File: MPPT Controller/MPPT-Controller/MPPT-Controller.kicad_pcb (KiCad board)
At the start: 4 copper layers, 81 parts, among them J1 Conn_01x02_Pin, J2 Conn_01x02_Pin, J3 Conn_01x02_Pin, J4 Conn_01x02_Pin, J5 USB_C_Receptacle_USB2.0_16P, J6 Conn_01x02_Pin, M1 Fan_4pin, Q1 IRL540N, SW1 SW_SPDT, U1 ADS1115IDGS, U2 ESP32-WROOM-32D, U3 CH340C, U4 LM1117DT-3.3, U5 LM2596S-ADJ, U6 TC4422, U7 ADS1115IDGS

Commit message: Layout
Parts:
- moved LR4 13.6 mm to (110.6, 106.7), turned to 90 degrees
- moved J2 11.2 mm to (121.9, 118.8)
- moved LR3 4.57 mm to (110.6, 119.0), turned to 90 degrees
- moved D10 1.98 mm to (179.8, 85.1)
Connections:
- HS1 pad 1: GND -> VinterA
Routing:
- added copper zone on F.Cu, net Net-(LR3-Pad2)
- added copper zone on F.Cu, net VinterB
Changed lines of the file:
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@@
 	(footprint "Diode_SMD:D_SMC"
 		(layer "F.Cu")
-		(at 177.915 84.585)
+		(at 179.832 85.09)
 		(descr "Diode SMC (DO-214AB)")
 		(tags "Diode SMC (DO-214AB)")
@@
 	(footprint "TerminalBlock:TerminalBlock_Altech_AK300-2_P5.00mm"
 		(layer "F.Cu")
-		(at 133.05 119.91 -90)
+		(at 121.92 118.85 -90)
 		(descr "Altech AK300 terminal block, pitch 5.0mm, 45 degree angled, see http://www.mouser.com/ds/2/16/PCBMETRC-24178.pdf")
 		(tags "Altech AK300 terminal block pitch 5.0mm")
@@
 	(footprint "Resistor_SMD:R_4020_10251Metric"
 		(layer "F.Cu")
-		(at 106.38 117.29)
+		(at 110.617 118.999 90)
 		(descr "Resistor SMD 4020 (10251 Metric), square (rectangular) end terminal, IPC-7351 nominal, (Body size source: http://datasheet.octopart.com/HVC0603T5004FET-Ohmite-datasheet-26699797.pdf), generated with kicad-footprint-generator")
 		(tags "resistor")
 		(property "Reference" "LR3"
-			(at 0 -3.6 0)
+			(at 0 -3.6 90)
 			(layer "F.SilkS")
 			(effects
@@
 		)
 		(property "Value" "0.1R"
-			(at 0 3.6 0)
+			(at 0 3.6 90)
 			(layer "F.Fab")
 			(effects
@@
 		)
 		(property "Datasheet" ""
-			(at 0 0 0)
+			(at 0 0 90)
 			(layer "F.Fab")
 			(hide yes)
@@
 		)
 		(property "Description" "Resistor"
-			(at 0 0 0)
+			(at 0 0 90)
 			(layer "F.Fab")
 			(hide yes)
@@
 		)
 		(fp_line
-			(start -5.8 -2.9)
-			(end 5.8 -2.9)
+			(start 5.8 -2.9)
+			(end 5.8 2.9)
 			(stroke
 				(width 0.05)
@@
 		)
 		(fp_line
-			(start -5.8 2.9)
-			(end -5.8 -2.9)
+			(start -5.8 -2.9)
+			(end 5.8 -2.9)
 			(stroke
 				(width 0.05)
@@
 		)
 		(fp_line
-			(start 5.8 -2.9)
-			(end 5.8 2.9)
+			(start 5.8 2.9)
+			(end -5.8 2.9)
 			(stroke
 				(width 0.05)
@@
 		)
 		(fp_line
-			(start 5.8 2.9)
-			(end -5.8 2.9)
+			(start -5.8 2.9)
+			(end -5.8 -2.9)
 			(stroke
 				(width 0.05)
@@
 		)
 		(fp_line
-			(start -5.1 -2.55)
-			(end 5.1 -2.55)
+			(start 5.1 -2.55)
+			(end 5.1 2.55)
 			(stroke
 				(width 0.1)
@@
 		)
 		(fp_line
-			(start -5.1 2.55)
-			(end -5.1 -2.55)
+			(start -5.1 -2.55)
+			(end 5.1 -2.55)
 			(stroke
 				(width 0.1)
@@
 		)
 		(fp_line
-			(start 5.1 -2.55)
-			(end 5.1 2.55)
+			(start 5.1 2.55)
+			(end -5.1 2.55)
 			(stroke
 				(width 0.1)
@@
 		)
 		(fp_line
-			(start 5.1 2.55)
-			(end -5.1 2.55)
+			(start -5.1 2.55)
+			(end -5.1 -2.55)
 			(stroke
 				(width 0.1)
@@
 		)
 		(fp_text user "${REFERENCE}"
-			(at 0 0 0)
+			(at 0 0 90)
 			(layer "F.Fab")
 			(effects
@@
 		)
 		(pad "1" smd roundrect
-			(at -4.8125 0)
+			(at -4.8125 0 90)
 			(size 1.475 5.3)
 			(layers "F.Cu" "F.Mask" "F.Paste")
@@
 		)
 		(pad "2" smd roundrect
-			(at 4.8125 0)
+			(at 4.8125 0 90)
 			(size 1.475 5.3)
 			(layers "F.Cu" "F.Mask" "F.Paste")
@@
 	(footprint "Resistor_SMD:R_4020_10251Metric"
 		(layer "F.Cu")
-		(at 119.08 117.29)
+		(at 110.617 106.68 90)
 		(descr "Resistor SMD 4020 (10251 Metric), square (rectangular) end terminal, IPC-7351 nominal, (Body size source: http://datasheet.octopart.com/HVC0603T5004FET-Ohmite-datasheet-26699797.pdf), generated with kicad-footprint-generator")
 		(tags "resistor")
 		(property "Reference" "LR4"
-			(at 0 -3.6 0)
+			(at 0 -3.6 90)
 			(layer "F.SilkS")
 			(effects
@@
 		)
 		(property "Value" "0.1R"
-			(at 0 3.6 0)
+			(at 0 3.6 90)
 			(layer "F.Fab")
 			(effects
@@
 		)
 		(property "Datasheet" ""
-			(at 0 0 0)
+			(at 0 0 90)
 			(layer "F.Fab")
 			(hide yes)
@@
 		)
 		(property "Description" "Resistor"
-			(at 0 0 0)
+			(at 0 0 90)
 			(layer "F.Fab")
 			(hide yes)
@@
 		)
 		(fp_line
-			(start -5.8 -2.9)
-			(end 5.8 -2.9)
+			(start 5.8 -2.9)
+			(end 5.8 2.9)
 			(stroke
 				(width 0.05)
@@
 		)
 		(fp_line
-			(start -5.8 2.9)
-			(end -5.8 -2.9)
+			(start -5.8 -2.9)
+			(end 5.8 -2.9)
 			(stroke
 				(width 0.05)
@@
 		)
 		(fp_line
-			(start 5.8 -2.9)
-			(end 5.8 2.9)
+			(start 5.8 2.9)
+			(end -5.8 2.9)
 			(stroke
 				(width 0.05)
@@
 		)
 		(fp_line
-			(start 5.8 2.9)
-			(end -5.8 2.9)
+			(start -5.8 2.9)
+			(end -5.8 -2.9)
 			(stroke
 				(width 0.05)
@@
 		)
 		(fp_line
-			(start -5.1 -2.55)
-			(end 5.1 -2.55)
+			(start 5.1 -2.55)
+			(end 5.1 2.55)
 			(stroke
 				(width 0.1)
@@
 		)
 		(fp_line
-			(start -5.1 2.55)
-			(end -5.1 -2.55)
+			(start -5.1 -2.55)
+			(end 5.1 -2.55)
 			(stroke
 				(width 0.1)
@@
 		)
 		(fp_line
-			(start 5.1 -2.55)
-			(end 5.1 2.55)
+			(start 5.1 2.55)
+			(end -5.1 2.55)
 			(stroke
 				(width 0.1)
@@
 		)
 		(fp_line
-			(start 5.1 2.55)
-			(end -5.1 2.55)
+			(start -5.1 2.55)
+			(end -5.1 -2.55)
 			(stroke
 				(width 0.1)
@@
 		)
 		(fp_text user "${REFERENCE}"
-			(at 0 0 0)
+			(at 0 0 90)
 			(layer "F.Fab")
 			(effects
@@
 		)
 		(pad "1" smd roundrect
-			(at -4.8125 0)
+			(at -4.8125 0 90)
 			(size 1.475 5.3)
 			(layers "F.Cu" "F.Mask" "F.Paste")
@@
 		)
 		(pad "2" smd roundrect
-			(at 4.8125 0)
+			(at 4.8125 0 90)
 			(size 1.475 5.3)
 			(layers "F.Cu" "F.Mask" "F.Paste")
@@
 			(layers "*.Cu" "*.Mask")
 			(remove_unused_layers no)
-			(net 2 "GND")
+			(net 4 "VinterA")
 			(pintype "passive")
 		)
@@
 		(polygon
 			(pts
-				(xy 54.356 109.474) (xy 59.944 109.474) (xy 59.944 116.332) (xy 54.356 116.332)
+				(xy 54.356 108.966) (xy 59.944 108.966) (xy 59.944 116.713) (xy 54.356 116.713)
+			)
+		)
+	)
+	(zone
+		(net 38)
+		(net_name "Net-(LR3-Pad2)")
+		(layer "F.Cu")
+		(hatch edge 0.5)
+		(priority 10)
+		(connect_pads yes
+			(clearance 0.75)
+		)
+		(min_thickness 0.25)
+		(filled_areas_thickness no)
+		(fill yes
+			(thermal_gap 0)
+			(thermal_bridge_width 1)
+		)
+		(polygon
+			(pts
+				(xy 107.696 108.966) (xy 107.696 116.713) (xy 113.538 116.713) (xy 113.538 108.966)
 			)
 		)
@@
 		(polygon
 			(pts
-				(xy 54.102 122.428) (xy 54.102 122.428) (xy 54.102 125.222) (xy 69.596306 125.222) (xy 69.60486 103.892696)
-				(xy 64.389 103.886) (xy 64.389 120.142) (xy 54.102 120.142)
+				(xy 54.102 122.428) (xy 54.102 122.428) (xy 54.102 125.222) (xy 72.898306 125.222) (xy 72.910047 95.946488)
+				(xy 64.389 95.935548) (xy 64.389 118.11) (xy 54.102 118.11)
+			)
+		)
+	)
+	(zone
+		(net 6)
+		(net_name "VinterB")
+		(layer "F.Cu")
+		(hatch edge 0.5)
+		(priority 11)
+		(connect_pads yes
+			(clearance 0.75)
+		)
+		(min_thickness 0.25)
+		(filled_areas_thickness no)
+		(fill yes
+			(thermal_gap 0)
+			(thermal_bridge_width 1)
+		)
+		(polygon
+			(pts
+				(xy 97.79 125.222) (xy 97.79 117.221) (xy 86.487 117.221) (xy 86.487 101.6) (xy 105.664 101.6) (xy 105.664 118.11)
+				(xy 113.665 118.11) (xy 113.665 125.222)
 			)
 		)
@@
 		(polygon
 			(pts
-				(xy 70.358 104.394) (xy 74.93 104.394) (xy 74.93 118.618) (xy 96.266 118.618) (xy 96.266 125.222)
+				(xy 70.358 104.394) (xy 74.93 104.394) (xy 74.93 118.491) (xy 96.266 118.491) (xy 96.266 125.222)
 				(xy 70.104 125.222) (xy 70.104 104.394)
 			)
@@
 		(polygon
 			(pts
-				(xy 52.324 99.314) (xy 34.544 99.314) (xy 34.544 106.807) (xy 60.198 106.807) (xy 60.198 99.314)
+				(xy 52.324 99.314) (xy 34.544 99.314) (xy 34.544 107.696) (xy 60.198 107.696) (xy 60.198 99.314)
 			)
 		)
@@
 		(polygon
 			(pts
-				(xy 70.1 104.4) (xy 74.93 104.4) (xy 74.93 118.62) (xy 96.26 118.62) (xy 96.26 125.224) (xy 70.1 125.224)
+				(xy 70.1 104.4) (xy 74.93 104.4) (xy 74.93 118.493) (xy 96.26 118.493) (xy 96.26 125.224) (xy 70.1 125.224)
 			)
 		)
@@
 		(polygon
 			(pts
-				(xy 61.468 104.394) (xy 67.31 104.394) (xy 67.31 110.49) (xy 80.01 110.49) (xy 80.01 119.38) (xy 61.468 119.126)
-				(xy 61.468 107.442)
+				(xy 61.468 104.394) (xy 67.31 104.394) (xy 67.31 107.315) (xy 85.09 107.315) (xy 85.09 119.449589)
+				(xy 61.468 119.126) (xy 61.468 107.442)
 			)
 		)

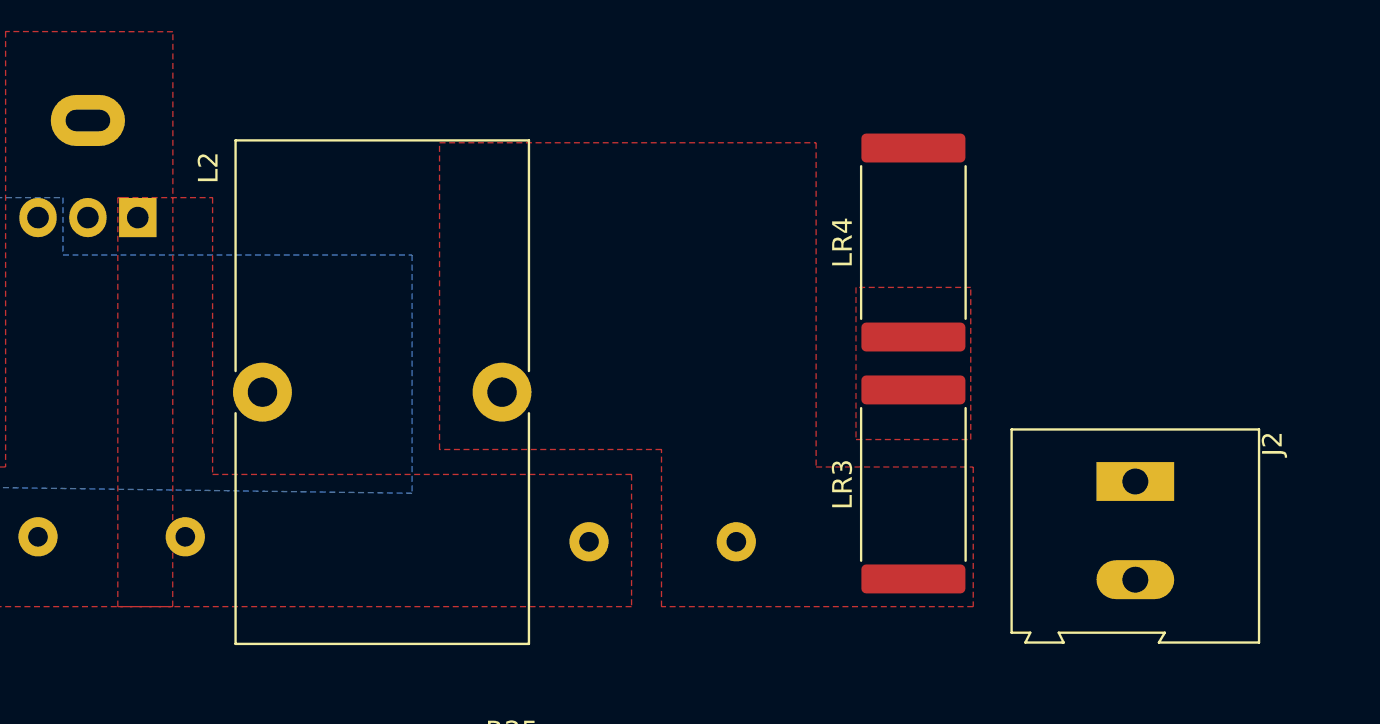
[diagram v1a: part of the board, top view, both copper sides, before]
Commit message: mask pullback
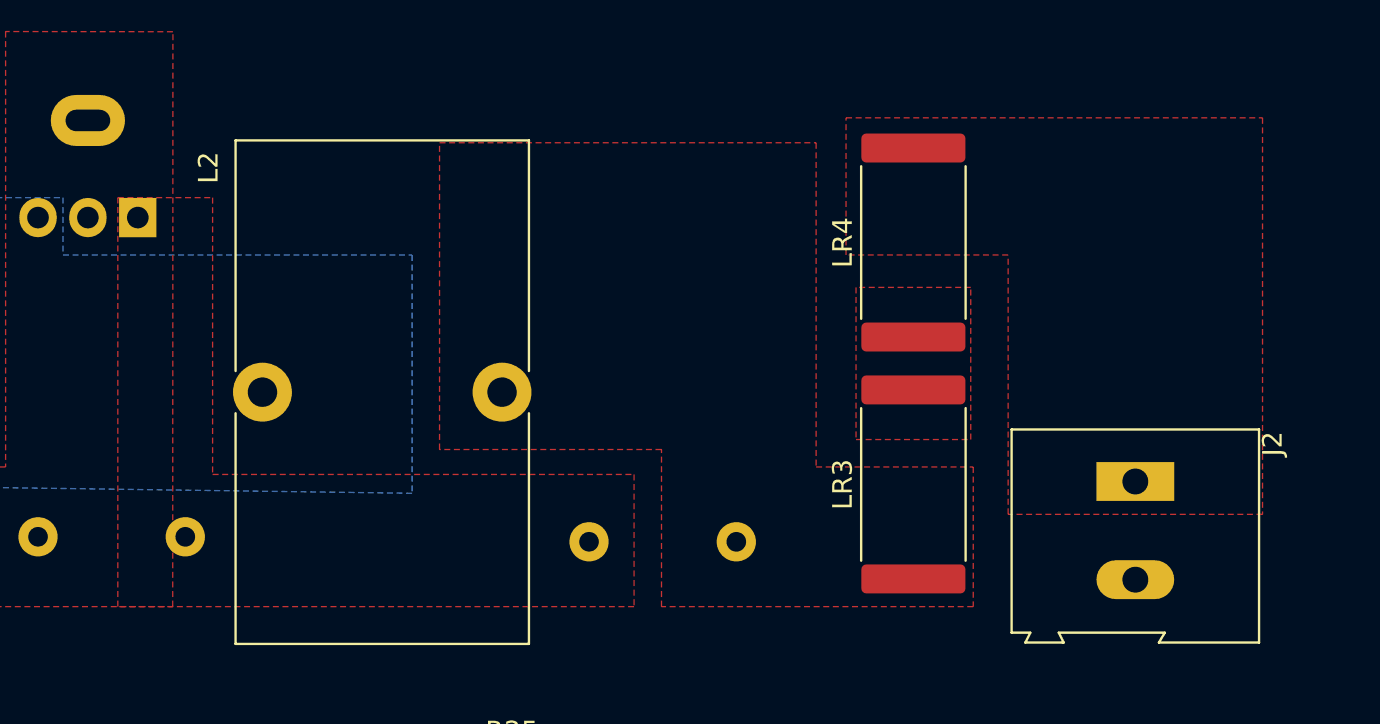
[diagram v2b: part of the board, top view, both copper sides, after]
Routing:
- added copper zone on F.Cu, net Vout
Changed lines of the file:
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@@
 		(polygon
 			(pts
-				(xy 70.358 104.394) (xy 74.93 104.394) (xy 74.93 118.491) (xy 96.266 118.491) (xy 96.266 125.222)
+				(xy 70.104 104.394) (xy 74.93 104.394) (xy 74.93 118.491) (xy 96.393 118.491) (xy 96.393 125.222)
 				(xy 70.104 125.222) (xy 70.104 104.394)
 			)
@@
 			(pts
 				(xy 52.324 99.314) (xy 34.544 99.314) (xy 34.544 107.696) (xy 60.198 107.696) (xy 60.198 99.314)
+			)
+		)
+	)
+	(zone
+		(net 7)
+		(net_name "Vout")
+		(layer "F.Cu")
+		(hatch edge 0.5)
+		(priority 13)
+		(connect_pads yes
+			(clearance 0.75)
+		)
+		(min_thickness 0.25)
+		(filled_areas_thickness no)
+		(fill yes
+			(thermal_gap 0)
+			(thermal_bridge_width 1)
+		)
+		(polygon
+			(pts
+				(xy 128.397 100.33) (xy 128.397 120.523) (xy 115.443 120.523) (xy 115.443 107.315) (xy 107.188 107.315)
+				(xy 107.188 100.33)
 			)
 		)
@@
 		(polygon
 			(pts
-				(xy 60.071 120.142) (xy 60.071 125.222) (xy 69.596 125.222) (xy 69.596 107.315) (xy 64.389 107.315)
+				(xy 64.389 120.142) (xy 64.389 125.222) (xy 69.342 125.222) (xy 69.342 107.315) (xy 64.389 107.315)
 				(xy 64.389 120.142)
 			)
@@
 		(polygon
 			(pts
-				(xy 70.1 104.4) (xy 74.93 104.4) (xy 74.93 118.493) (xy 96.26 118.493) (xy 96.26 125.224) (xy 70.1 125.224)
+				(xy 70.1 107.321) (xy 74.93 107.321) (xy 74.93 118.493) (xy 74.93 118.493) (xy 74.93 125.224) (xy 70.1 125.224)
 			)
 		)
